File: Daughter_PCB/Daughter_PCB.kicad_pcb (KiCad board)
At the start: 2 copper layers, 35.5 x 50 mm, 26 parts, among them J14 Analog 0, J15 Screw_Terminal_01x04, J16 Screw_Terminal_01x02, J17 Conn_01x08, J18 Conn_01x08, U3 AMS1117-3.3, U4 CD74HCT4067QM96Q, U5 OPA607Q1

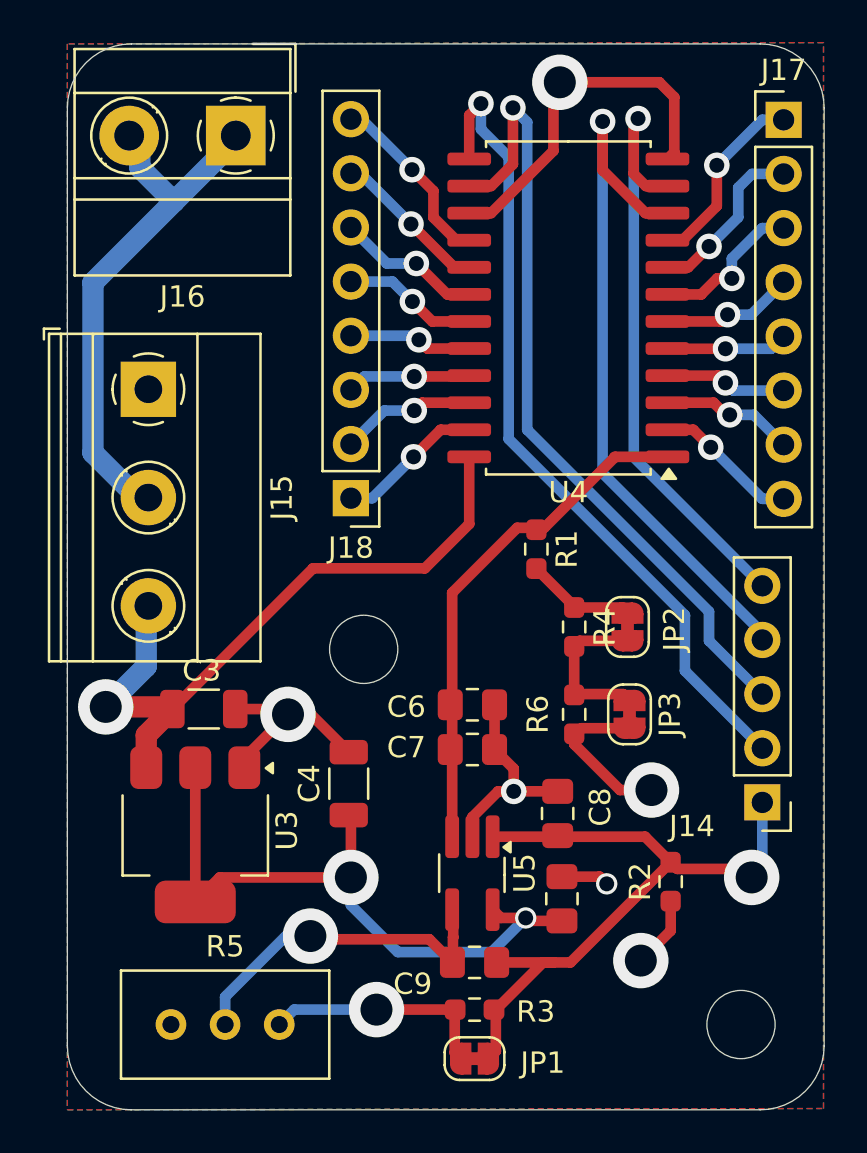
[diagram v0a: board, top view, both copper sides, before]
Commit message: Redid the analog multiplexer
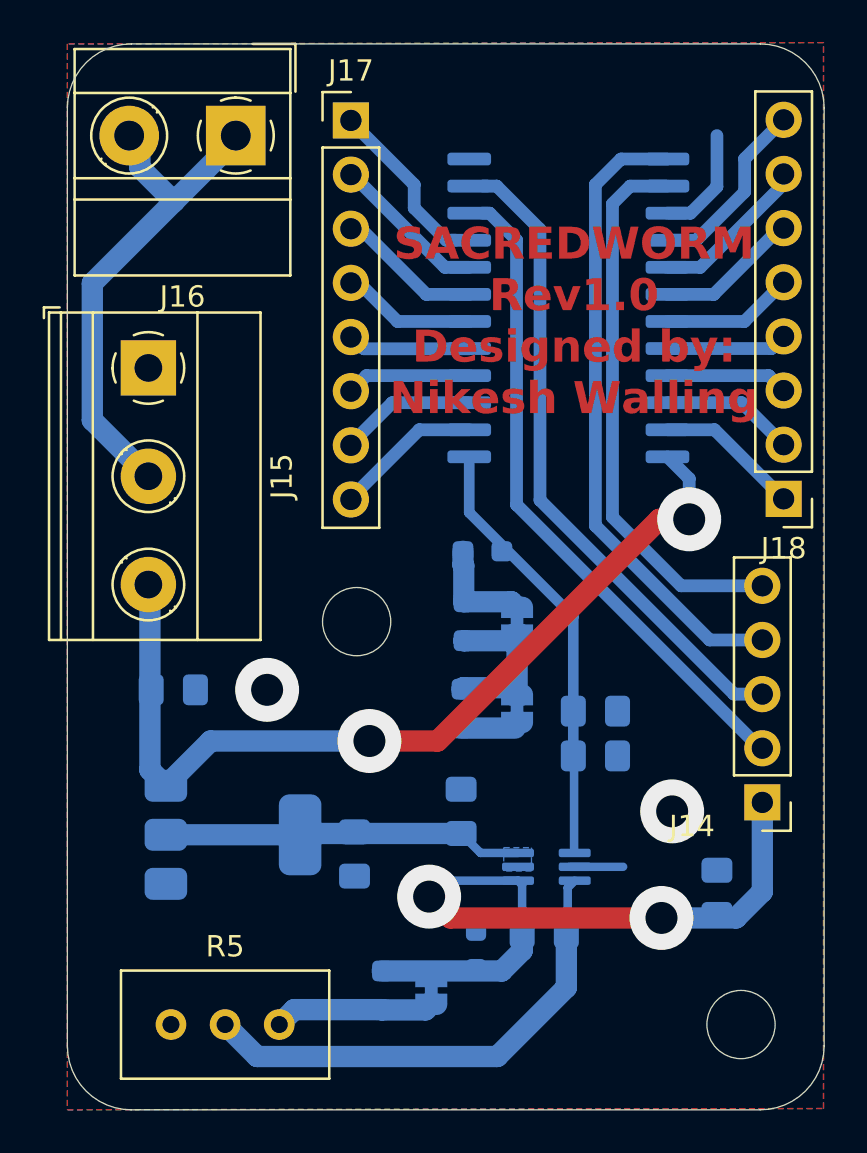
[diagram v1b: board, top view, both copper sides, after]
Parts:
- C3, C4: footprint Capacitor_SMD:C_1206_3216Metric -> Capacitor_SMD:C_0805_2012Metric_Pad1.18x1.45mm_HandSolder; moved to B.Cu
- C5, C6, C7, C8, C9, JP1, JP2, JP3, R1, R2, R3, R4, R6, U3, U4: moved to B.Cu
- U5: footprint Package_TO_SOT_SMD:TSOT-23-5_HandSoldering -> Package_TO_SOT_SMD:SOT-363_SC-70-6_Handsoldering; moved to B.Cu
- moved J17 20.3 mm to (100.5, 81.1)
- moved J18 20.3 mm to (120.8, 98.8)
- moved R2 9.67 mm to (106.4, 120.0), turned to -90 degrees
- moved C8 8.34 mm to (117.7, 117.3)
- moved C5 6.26 mm to (105.7, 113.5)
- moved C6 6.25 mm to (112.0, 110.9)
- moved C7 6.04 mm to (112.0, 108.8)
- moved JP3 5.28 mm to (108.3, 108.7)
- moved R6 5.28 mm to (105.7, 108.7)
- moved JP2 5.19 mm to (108.3, 104.6)
- moved R4 5.19 mm to (105.8, 104.6)
- moved R3 4.42 mm to (102.0, 121.9), turned to -90 degrees
- moved JP1 3.79 mm to (104.3, 121.9), turned to -90 degrees
- moved C9 3.55 mm to (109.6, 119.2), turned to 180 degrees
- moved U5 3.48 mm to (109.7, 116.1), turned to 180 degrees
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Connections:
- J14 pad 2: /MUX_3 -> /MUX_0
- J14 pad 3: /MUX_2 -> /MUX_1
- J14 pad 4: /MUX_0 -> /MUX_3
- J14 pad 5: /MUX_1 -> /MUX_2
- U5 pad 1: /Analog_0 -> Net-(U4-COM)
- U5 pad 3: Net-(U4-COM) -> Net-(U5--)
- U5 pad 4: Net-(U5--) -> /Analog_0
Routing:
- net GND: track 49.3 -> 10.2 mm, vias 6 -> 2
- net +3.3V: track 31.2 -> 16.8 mm, vias 2 -> 0
- net /MUX_2: track 37.5 -> 26.0 mm, vias 1 -> 0
- net +5V: track 32.2 -> 42.9 mm, vias 1 -> 2
- net /MUX_3: track 38.5 -> 29.9 mm, vias 1 -> 0
- net Net-(U5--): track 16.1 -> 22.7 mm, vias 1 -> 0
- net Net-(U4-COM): track 24.2 -> 20.5 mm
- net Net-(JP1-B): track 10.9 -> 7.53 mm, vias 1 -> 0
- net /MUX_0: track 33.6 -> 30.8 mm, vias 1 -> 0
- net /Analog_0: track 32.8 -> 35.5 mm, vias 1 -> 2
- net /MUX_1: track 28.6 -> 30.5 mm, vias 1 -> 0
- net +12V: track 25.9 -> 24.9 mm
- net Net-(J17-Pin_1): track 8.91 -> 8.00 mm, vias 1 -> 0
- net Net-(J17-Pin_3): track 7.28 -> 6.45 mm, vias 1 -> 0
- net Net-(J17-Pin_2): track 8.08 -> 7.38 mm, vias 1 -> 0
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- added copper zone on B.Cu, net +3.3V
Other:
- board text added: "SACREDWORM Rev1.0 Designed by: Nikesh Walling"
